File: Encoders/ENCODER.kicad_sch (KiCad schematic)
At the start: 5 parts

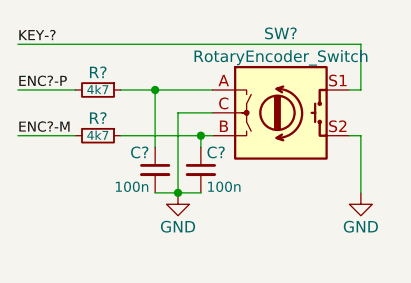
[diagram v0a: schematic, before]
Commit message: Fix grid alignment and update to KiCad 9
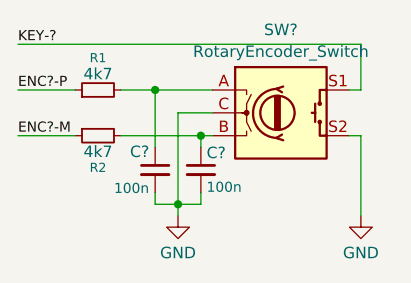
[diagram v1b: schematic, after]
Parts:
- removed C?: 100n, symbol Device:C_Small
- removed R? (x2): 4k7, symbol Device:R_Small
- added C?: 100n, symbol Device:C_Small
- added R1, R2: 4k7, symbol Device:R_Small
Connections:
- net ENC?-M: now also R2.1
- net ENC?-P: now also R1.1
- net GND: now also C?.2
- net at C?.1, SW?.B: now also R2.2
- net at SW?.A: now also C?.1, R1.2
